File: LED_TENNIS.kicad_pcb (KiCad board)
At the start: 2 copper layers, 101.6 x 70.6 mm, 16 parts, among them J1 USB_B, U1 ATmega328P-PU, Y1 Crystal

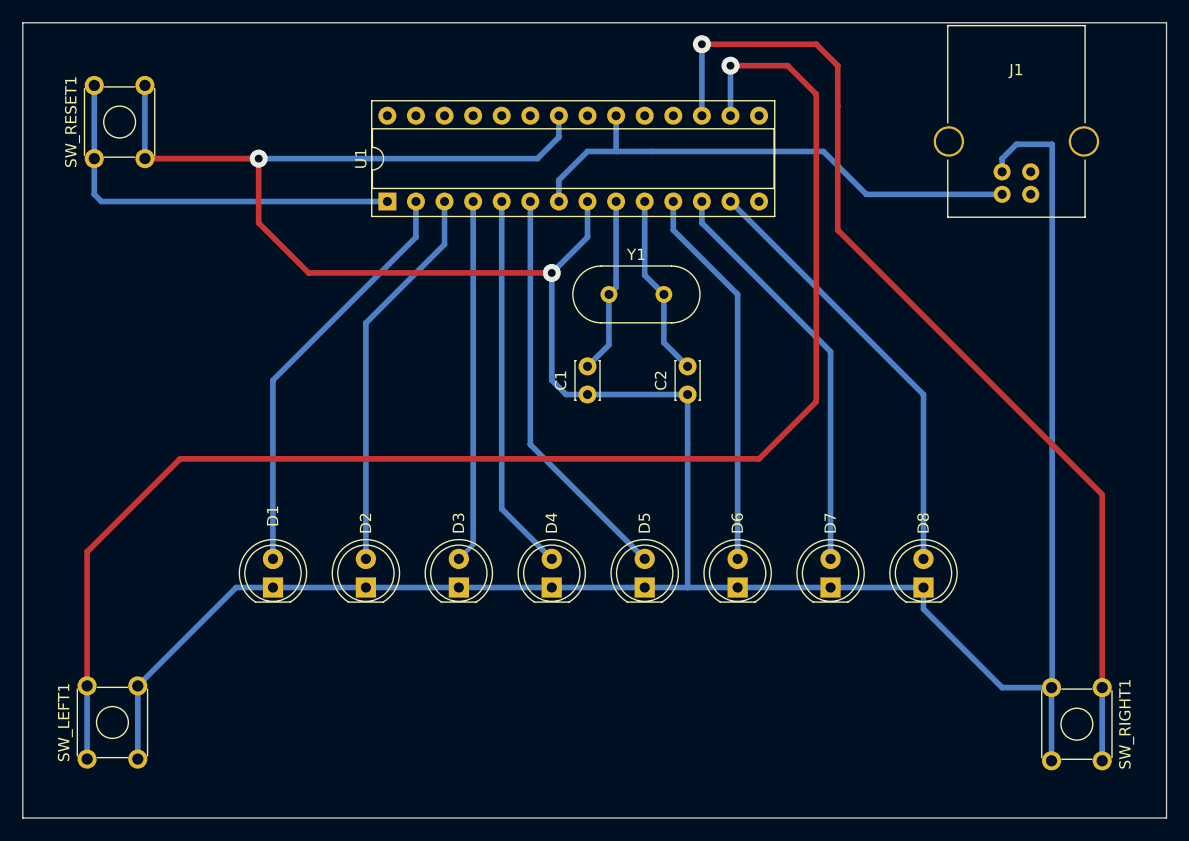
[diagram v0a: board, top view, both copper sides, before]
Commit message: Add files via upload
increased the size of the traces to facilitate easier toner transfer
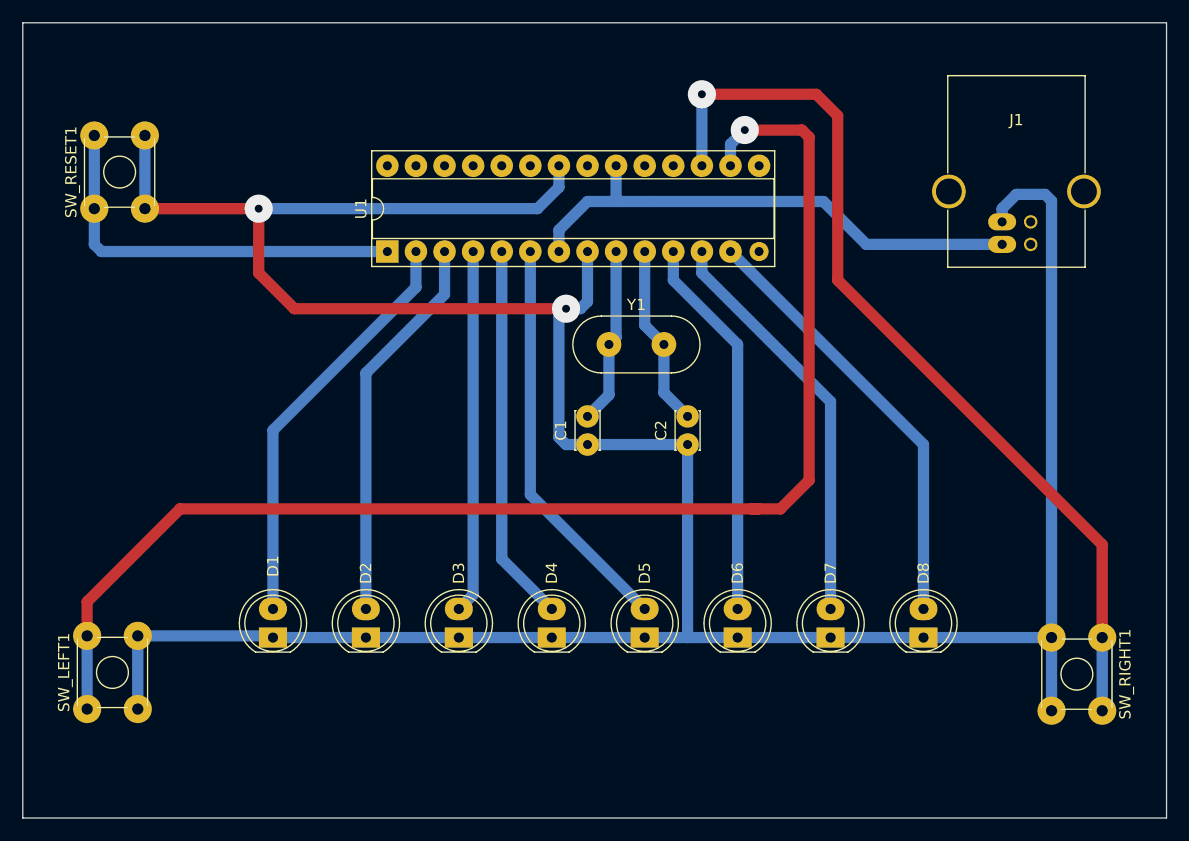
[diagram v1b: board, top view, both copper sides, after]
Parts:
- moved C1 4.45 mm to (161.3, 94.0)
- moved C2 4.45 mm to (170.2, 94.0)
- moved J1 4.45 mm to (198.1, 76.2)
- moved SW_LEFT1 4.45 mm to (116.8, 117.5)
- moved SW_RESET1 4.45 mm to (117.5, 73.0)
- moved Y1 4.45 mm to (163.2, 85.1)
- moved D1 4.44 mm to (133.3, 111.1)
- moved D2 4.44 mm to (141.6, 111.1)
- moved D3 4.44 mm to (149.9, 111.1)
- moved D4 4.44 mm to (158.1, 111.1)
- moved D5 4.44 mm to (166.4, 111.1)
- moved D6 4.44 mm to (174.6, 111.1)
- moved D7 4.44 mm to (182.9, 111.1)
- moved D8 4.44 mm to (191.1, 111.1)
- moved SW_RIGHT1 4.44 mm to (207.0, 111.1)
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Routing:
- net GND: track 283.5 -> 266.9 mm
- net /SW_LEFT: track 129.1 -> 118.9 mm
- net /SW_RIGHT: track 90.7 -> 81.8 mm
